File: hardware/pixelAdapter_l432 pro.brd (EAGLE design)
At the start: 26.9 x 34.9 mm, 37 parts, among them U1 SN74HCT245PWR, U2 AP2120N-3.3TRG1, U3 STM32L432KCU6

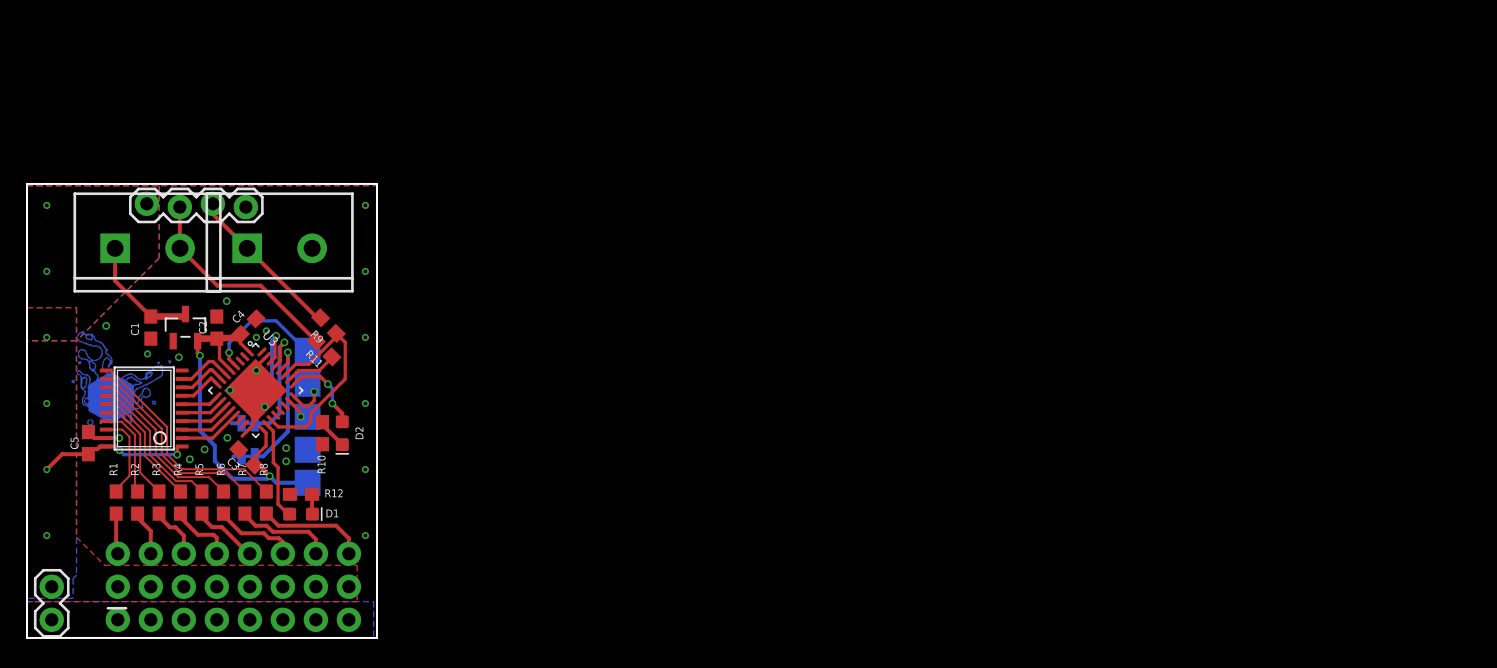
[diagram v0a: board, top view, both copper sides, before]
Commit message: hardware files for variants, limit max transfer bits
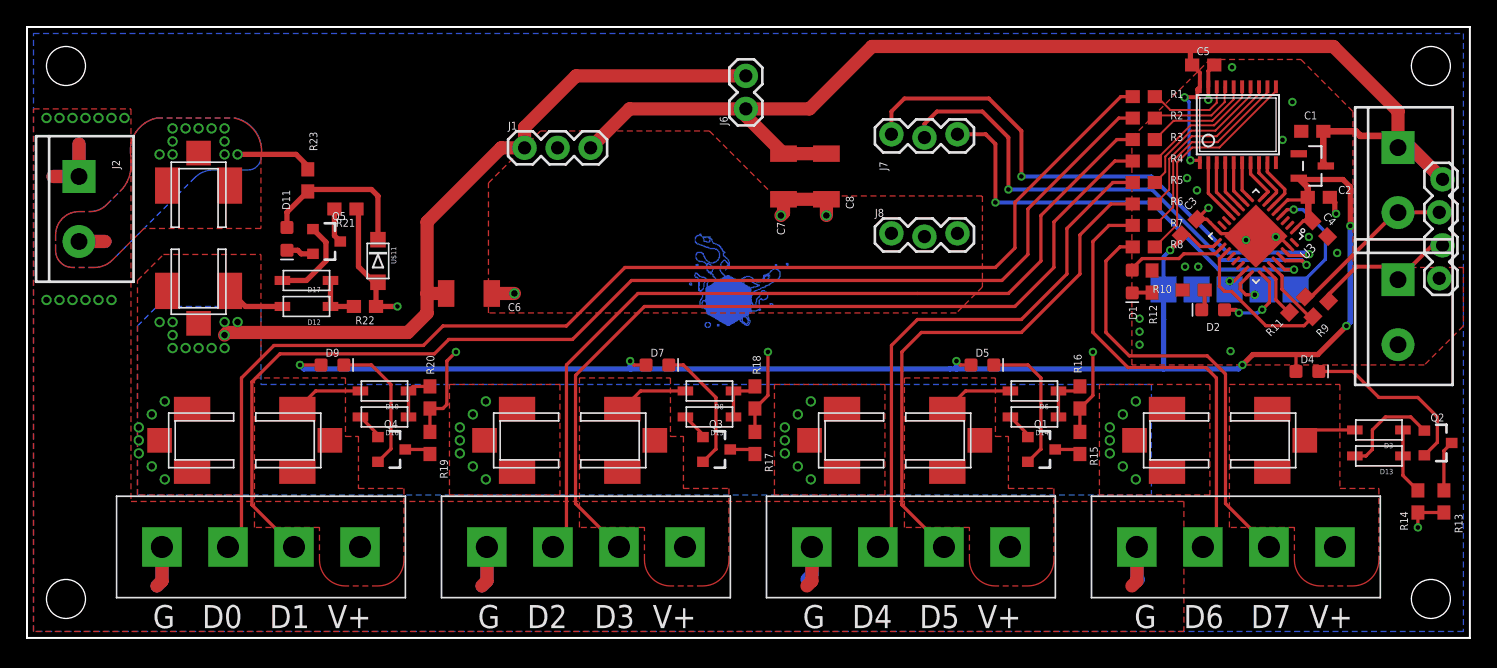
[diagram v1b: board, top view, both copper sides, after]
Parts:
- removed JP1, JP2, JP3: JUMPER-SMT_2_NC_TRACE_SILK, SparkFun-Jumpers:SMT-JUMPER_2_NC_TRACE_SILK
- added C6: 10uF, SparkFun-Capacitors:1210
- added C7, C8: 22uF, SparkFun-Capacitors:1210
- added D10, D12, D13, D14, D15, D16, D17, D3, D6, D8: (no value), adafruit:SOD-123
- added D11, D4, D5, D7, D9: RED, SparkFun-LED:LED-0603
- added J7, J8: (no value), SparkFun-Connectors:1X03_LOCK
- added Q1, Q2, Q3, Q4, Q5: 200mA/40V, SparkFun-DiscreteSemi:SOT23-3
- added R13, R15, R17, R19, R21: 330, SparkFun-Resistors:0603
- added R14, R16, R18, R20, R22: 10k, SparkFun-Resistors:0603
- added R23: 1.5k, SparkFun-Resistors:0603
- added U$1, U$3, U$5, U$6: CON4-508, bens:CON4-508
- added U$10, U$4, U$7, U$8, U$9: FUSE, bens:KEYSTONE-3586-FUSEHOLDER
- added U$11: ZENER-3.3V, bens:SOD-123FL
- J1: device SparkFun-Connectors:1X08_NO_SILK -> SparkFun-Connectors:1X03
- J2: device bens:2X8-NOSILK -> bens:SCREWTERMINAL-5MM-2
- moved J3 99.0 mm to (105.5, 37.7), turned to 270 degrees
- moved J5 92.1 mm to (108.8, 27.7), turned to 90 degrees
- moved C1 90.6 mm to (98.9, 39.0), turned to 180 degrees
- moved C5 90.6 mm to (90.5, 44.1), turned to 0 degrees
- moved J4 88.6 mm to (105.5, 27.6), turned to 270 degrees
- moved U2 87.6 mm to (98.9, 36.3), turned to 270 degrees
- moved U1 86.9 mm to (93.2, 39.5), turned to 0 degrees
- moved C2 85.4 mm to (99.4, 33.9), turned to 0 degrees
- moved R1 85.0 mm to (85.9, 41.6), turned to 180 degrees
- moved R2 82.9 mm to (85.9, 40.0), turned to 180 degrees
- moved C4 82.8 mm to (99.5, 31.5), turned to 315 degrees
- moved R3 80.7 mm to (85.9, 38.3), turned to 180 degrees
- moved R4 78.6 mm to (85.9, 36.7), turned to 180 degrees
- moved U3 77.9 mm to (94.5, 30.9), turned to 225 degrees
- moved R5 76.5 mm to (85.9, 35.0), turned to 180 degrees
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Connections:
- removed net JP1: JP1.1, U3.30
- removed net JP2: JP2.1, U3.29
- removed net JP3: JP3.2, U3.28
- new net ADDR0: J7.1, U3.30
- new net ADDR1: J7.2, U3.29
- new net ADDR2: J7.3, U3.28
- new net N$1: D17.A, Q5.1
- new net N$10: D5.C, Q1.2
- new net N$11: Q1.3, R15.2
- new net N$20: D11.A, R23.1, U$11.C
- new net N$22: D15.C, D8.C, R18.2
- new net N$23: D7.C, Q3.2
- new net N$24: Q3.3, R17.2
- new net N$25: D13.A, Q2.1
- new net N$26: D10.C, D16.C, R20.2
- new net N$27: D9.C, Q4.2
- new net N$28: Q4.3, R19.2
- new net N$29: D14.A, Q1.1
- new net N$3: D12.C, D17.C, R22.2
- new net N$30: D15.A, Q3.1
- new net N$31: D16.A, Q4.1
- new net N$4: D13.C, D3.C, R14.2
- new net N$5: D4.C, Q2.2
- new net N$6: D11.C, Q5.2
- new net N$7: Q2.3, R13.2
- new net N$8: Q5.3, R21.2
- new net N$9: D14.C, D6.C, R16.2
- new net POWER+: J2.2, R23.2, U$10.A1, U$10.A2, U$10.A3
- new net VIN: C6.1, D12.A, J1.1, J6.2, U$10.B1, U$10.B2, U$10.B3, U$4.A1, U$4.A2, U$4.A3, U$7.A1, U$7.A2, U$7.A3, U$8.A1, U$8.A2, U$8.A3, U$9.A1, U$9.A2, U$9.A3
- new net VOUT1: D3.A, U$1.4, U$4.B1, U$4.B2, U$4.B3
- new net VOUT2: D6.A, U$3.4, U$7.B1, U$7.B2, U$7.B3
- new net VOUT3: D8.A, U$5.4, U$8.B1, U$8.B2, U$8.B3
- new net VOUT4: D10.A, U$6.4, U$9.B1, U$9.B2, U$9.B3
- net +3V3: now also D4.A, D5.A, D7.A, D9.A
- net 5V: now also C7.2, C8.2, J1.3, J6.1; no longer J2.1, J2.11, J2.13, J2.15, J2.3, J2.5, J2.7, J2.9, J6.2
- net GND: now also C6.2, C7.1, C8.1, J2.1, J8.1, J8.2, J8.3, R13.1, R14.1, R15.1, R16.1, R17.1, R18.1, R19.1, R20.1, R21.1, R22.1, U$1.1, U$11.A, U$3.1, U$5.1, U$6.1; no longer J1.1, J1.3, J1.4, J1.5, J1.6, J1.7, J1.8, J6.1, JP1.2, JP2.2, JP3.1
- net LED0: now also U$6.2; no longer J2.2
- net LED1: now also U$6.3; no longer J2.4
- net LED2: now also U$5.2; no longer J2.6
- net LED3: now also U$5.3; no longer J2.8
- net LED4: now also U$3.2; no longer J2.10
- net LED5: now also U$3.3; no longer J2.12
- net LED6: now also U$1.2; no longer J2.14
- net LED7: now also U$1.3; no longer J2.16
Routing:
- net +3V3: track 30.6 -> 129.5 mm, vias 2 -> 7
- net LED0: track 3.14 -> 93.0 mm
- net LED1: track 3.51 -> 92.3 mm
- net 5V: track 21.1 -> 107.3 mm, vias 8 -> 2
- net GND: track 10.2 -> 86.7 mm, vias 21 -> 39
- net LED2: track 4.13 -> 67.2 mm
- net LED3: track 4.96 -> 66.3 mm
- net VIN: track 0.00 -> 59.7 mm, vias 0 -> 39
- net ADDR0: track 0.00 -> 43.3 mm, vias 0 -> 2
- net ADDR1: track 0.00 -> 40.3 mm, vias 0 -> 2
- net LED4: track 5.12 -> 41.7 mm
- net ADDR2: track 0.00 -> 34.5 mm, vias 0 -> 2
- net LED5: track 6.45 -> 40.6 mm
- net LED6: track 7.46 -> 35.0 mm
- net LED7: track 8.32 -> 33.2 mm
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- added copper zone on layer 1, net POWER+
- added copper zone on layer 16, net POWER+
- added copper zone on layer 1, net VIN
- added copper zone on layer 16, net VIN
- added copper zone on layer 1, net VOUT1
- added copper zone on layer 1, net VOUT2
- added copper zone on layer 1, net VOUT3
- added copper zone on layer 1, net VOUT4
- removed copper zone on layer 1, net 5V
- removed copper zone on layer 16, net 5V
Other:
- board size 26.9 x 34.9 mm -> 111 x 47 mm
- board text added: "G D0 D1 V+"
- board text added: "G D2 D3 V+"
- board text added: "G D4 D5 V+"
- board text added: "G D6 D7 V+"
- board text added: "Set Addr"
- board text added: "VIN"
- board text added: "VIN to 5V Converter"
- board text added: "electromage.com Output Expander Pro Mini v3.1 ©2021 Ben Hencke"
- board text removed: "0"
- board text removed: "3"
- board text removed: "5"
- board text removed: "6"
- board text removed: "7"
- board text removed: "Address Setting"
- board text removed: "Data"
- board text removed: "JP1"
- board text removed: "JP2"
- board text removed: "JP3"
- board text removed: "Output Expander"
- board text removed: "electromage.com Output Expander v3.0 ©2021 Ben Hencke"
- board text removed: "v3.0 ©2021 Ben Hencke"
